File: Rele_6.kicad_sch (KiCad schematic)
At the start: 6 parts, among them J18 Rele_6, J36 Pin GND, K7 SRD-05VDC-SL-C, Q15 PMBT3904,235

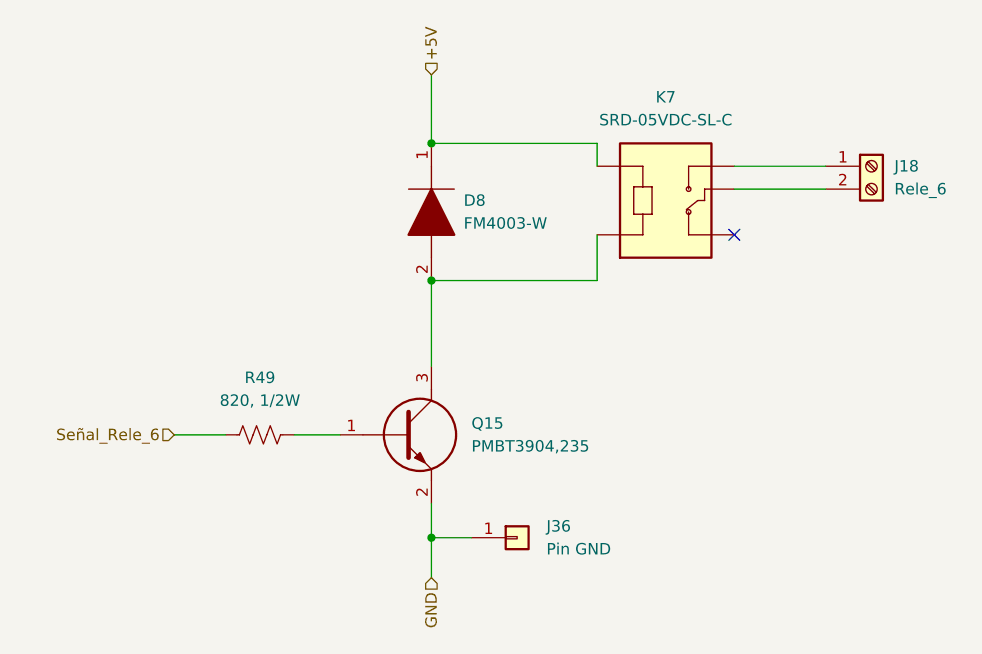
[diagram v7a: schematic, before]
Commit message: Se modificaron algunos componentes, según disponibilidad
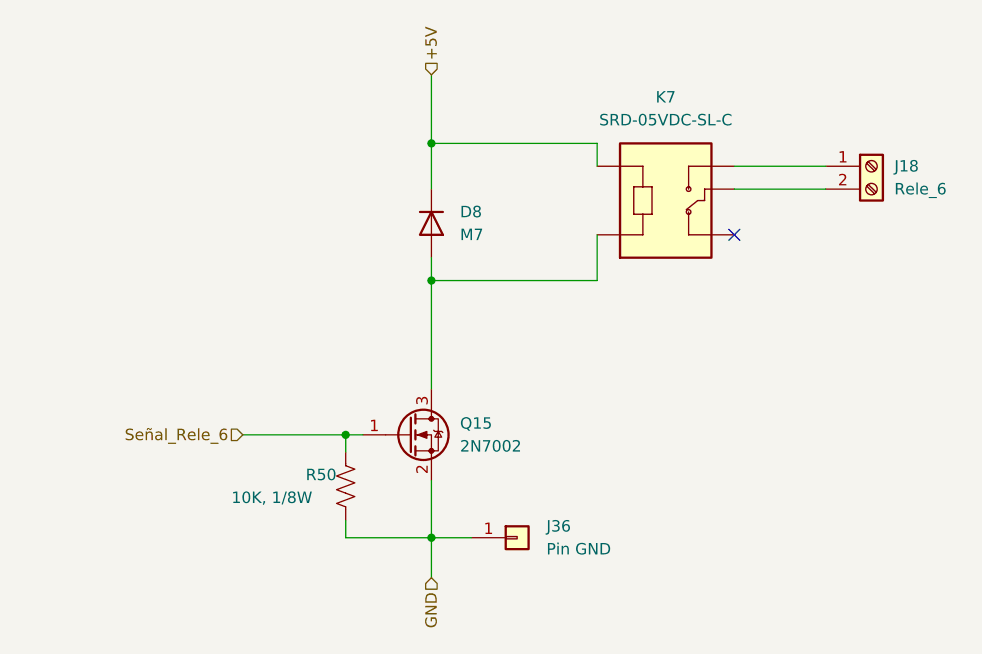
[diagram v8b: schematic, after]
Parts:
- removed D8: FM4003-W, FM4003W:DIOM5025X231N, symbol FM4003-W:FM4003-W
- removed Q15: PMBT3904,235, PMBT3904,235:SOT95P230X110-3N, symbol PMBT3904,235:PMBT3904,235
- removed R49: 820, 1/2W, Resistor_SMD:R_0805_2012Metric, symbol Device:R_US
- added D8: M7, Diode_SMD:D_SMA, symbol Device:D
- added Q15: 2N7002, Package_TO_SOT_SMD:SOT-23, symbol Transistor_FET:2N7002
- added R50: 10K, 1/8W, Resistor_SMD:R_0805_2012Metric, symbol Device:R_US
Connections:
- net +5V: now also D8.1 (K)
- net GND: now also Q15.2 (S), R50.2
- net Señal_Rele_6: now also Q15.1 (G), R50.1
- net at K7.A2: now also D8.2 (A), Q15.3 (D)
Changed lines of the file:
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@@
 (kicad_sch (version 20211123) (generator eeschema)
   (paper "A4")
+  (junction (at 137.16 107.315) (diameter 0) (color 0 0 0 0)
+  )
   (junction (at 146.685 118.745) (diameter 0) (color 0 0 0 0)
   )
+  (junction (at 146.685 90.17) (diameter 0) (color 0 0 0 0)
+  )
   (junction (at 146.685 74.93) (diameter 0) (color 0 0 0 0)
-  )
-  (junction (at 146.685 90.17) (diameter 0) (color 0 0 0 0)
   )
   (no_connect (at 180.34 85.09))
@@
     (stroke (width 0) (type default) (color 0 0 0 0))
   )
-  (wire (pts (xy 131.445 107.315) (xy 136.525 107.315))
+  (wire (pts (xy 137.16 116.84) (xy 137.16 118.745))
     (stroke (width 0) (type default) (color 0 0 0 0))
   )
-  (wire (pts (xy 146.685 114.935) (xy 146.685 118.745))
+  (wire (pts (xy 137.16 107.315) (xy 139.065 107.315))
+    (stroke (width 0) (type default) (color 0 0 0 0))
+  )
+  (wire (pts (xy 125.73 107.315) (xy 137.16 107.315))
+    (stroke (width 0) (type default) (color 0 0 0 0))
+  )
+  (wire (pts (xy 146.685 112.395) (xy 146.685 118.745))
     (stroke (width 0) (type default) (color 0 0 0 0))
   )
@@
     (stroke (width 0) (type default) (color 0 0 0 0))
   )
+  (wire (pts (xy 137.16 107.315) (xy 137.16 109.22))
+    (stroke (width 0) (type default) (color 0 0 0 0))
+  )
   (wire (pts (xy 146.685 67.31) (xy 146.685 74.93))
+    (stroke (width 0) (type default) (color 0 0 0 0))
+  )
+  (wire (pts (xy 146.685 74.93) (xy 146.685 80.01))
+    (stroke (width 0) (type default) (color 0 0 0 0))
+  )
+  (wire (pts (xy 146.685 87.63) (xy 146.685 90.17))
+    (stroke (width 0) (type default) (color 0 0 0 0))
+  )
+  (wire (pts (xy 137.16 118.745) (xy 146.685 118.745))
     (stroke (width 0) (type default) (color 0 0 0 0))
   )
@@
     (stroke (width 0) (type default) (color 0 0 0 0))
   )
-  (wire (pts (xy 118.11 107.315) (xy 123.825 107.315))
-    (stroke (width 0) (type default) (color 0 0 0 0))
-  )
-  (wire (pts (xy 146.685 90.17) (xy 146.685 99.695))
+  (wire (pts (xy 146.685 90.17) (xy 146.685 102.235))
     (stroke (width 0) (type default) (color 0 0 0 0))
   )
@@
     (effects (font (size 1.27 1.27)) (justify left))
   )
-  (hierarchical_label "Señal_Rele_6" (shape input) (at 118.11 107.315 180)
+  (hierarchical_label "Señal_Rele_6" (shape input) (at 125.73 107.315 180)
     (effects (font (size 1.27 1.27)) (justify right))
   )
-  (symbol (lib_id "Device:R_US") (at 127.635 107.315 90) (unit 1)
-    (in_bom yes) (on_board yes) (fields_autoplaced)
-    (property "Reference" "R49" (id 0) (at 127.635 100.965 90))
-    (property "Value" "820, 1/2W" (id 1) (at 127.635 103.505 90))
-    (property "Footprint" "Resistor_SMD:R_0805_2012Metric" (id 2) (at 127.889 106.299 90)
+  (symbol (lib_id "Device:R_US") (at 137.16 113.03 0) (unit 1)
+    (in_bom yes) (on_board yes)
+    (property "Reference" "R50" (id 0) (at 132.715 111.76 0)
+      (effects (font (size 1.27 1.27)) (justify left))
+    )
+    (property "Value" "10K, 1/8W" (id 1) (at 124.46 114.3 0)
+      (effects (font (size 1.27 1.27)) (justify left))
+    )
+    (property "Footprint" "Resistor_SMD:R_0805_2012Metric" (id 2) (at 138.176 113.284 90)
       (effects (font (size 1.27 1.27)) hide)
     )
-    (property "Datasheet" "~" (id 3) (at 127.635 107.315 0)
+    (property "Datasheet" "~" (id 3) (at 137.16 113.03 0)
       (effects (font (size 1.27 1.27)) hide)
     )
     (pin "1")
     (pin "2")
+  )
+  (symbol (lib_id "Transistor_FET:2N7002") (at 144.145 107.315 0) (unit 1)
+    (in_bom yes) (on_board yes) (fields_autoplaced)
+    (property "Reference" "Q15" (id 0) (at 149.86 106.0449 0)
+      (effects (font (size 1.27 1.27)) (justify left))
+    )
+    (property "Value" "2N7002" (id 1) (at 149.86 108.5849 0)
+      (effects (font (size 1.27 1.27)) (justify left))
+    )
+    (property "Footprint" "Package_TO_SOT_SMD:SOT-23" (id 2) (at 149.225 109.22 0)
+      (effects (font (size 1.27 1.27) italic) (justify left) hide)
+    )
+    (property "Datasheet" "https://www.onsemi.com/pub/Collateral/NDS7002A-D.PDF" (id 3) (at 144.145 107.315 0)
+      (effects (font (size 1.27 1.27)) (justify left) hide)
+    )
+    (pin "1")
+    (pin "2")
+    (pin "3")
   )
   (symbol (lib_id "Connector:Screw_Terminal_01x02") (at 195.58 77.47 0) (unit 1)
@@
     (pin "1")
     (pin "2")
-  )
-  (symbol (lib_id "FM4003-W:FM4003-W") (at 146.685 74.93 270) (unit 1)
-    (in_bom yes) (on_board yes) (fields_autoplaced)
-    (property "Reference" "D8" (id 0) (at 150.2664 81.2799 90)
-      (effects (font (size 1.27 1.27)) (justify left))
-    )
-    (property "Value" "FM4003-W" (id 1) (at 150.2664 83.8199 90)
-      (effects (font (size 1.27 1.27)) (justify left))
-    )
-    (property "Footprint" "FM4003W:DIOM5025X231N" (id 2) (at 146.685 86.36 0)
-      (effects (font (size 1.27 1.27)) (justify left) hide)
-    )
-    (property "Datasheet" "https://componentsearchengine.com/Datasheets/1/FM4003-W.pdf" (id 3) (at 144.145 86.36 0)
-      (effects (font (size 1.27 1.27)) (justify left) hide)
-    )
-    (property "Description" "Rectifiers 1A 200V GP" (id 4) (at 141.605 86.36 0)
-      (effects (font (size 1.27 1.27)) (justify left) hide)
-    )
-    (property "Height" "2.31" (id 5) (at 139.065 86.36 0)
-      (effects (font (size 1.27 1.27)) (justify left) hide)
-    )
-    (property "Manufacturer_Name" "Rectron" (id 6) (at 136.525 86.36 0)
-      (effects (font (size 1.27 1.27)) (justify left) hide)
-    )
-    (property "Manufacturer_Part_Number" "FM4003-W" (id 7) (at 133.985 86.36 0)
-      (effects (font (size 1.27 1.27)) (justify left) hide)
-    )
-    (property "Mouser Part Number" "583-FM4003-W" (id 8) (at 131.445 86.36 0)
-      (effects (font (size 1.27 1.27)) (justify left) hide)
-    )
-    (property "Mouser Price/Stock" "https://www.mouser.co.uk/ProductDetail/Rectron/FM4003-W/?qs=5h8Q3Z7TNRlJu6QU92Ho0w%3D%3D" (id 9) (at 128.905 86.36 0)
-      (effects (font (size 1.27 1.27)) (justify left) hide)
-    )
-    (property "Arrow Part Number" "FM4003-W" (id 10) (at 126.365 86.36 0)
-      (effects (font (size 1.27 1.27)) (justify left) hide)
-    )
-    (property "Arrow Price/Stock" "https://www.arrow.com/en/products/fm4003-w/rectron" (id 11) (at 123.825 86.36 0)
-      (effects (font (size 1.27 1.27)) (justify left) hide)
-    )
-    (property "Mouser Testing Part Number" "" (id 12) (at 121.285 86.36 0)
-      (effects (font (size 1.27 1.27)) (justify left) hide)
-    )
-    (property "Mouser Testing Price/Stock" "" (id 13) (at 118.745 86.36 0)
-      (effects (font (size 1.27 1.27)) (justify left) hide)
-    )
-    (pin "1")
-    (pin "2")
-  )
-  (symbol (lib_id "PMBT3904,235:PMBT3904,235") (at 136.525 107.315 0) (unit 1)
-    (in_bom yes) (on_board yes) (fields_autoplaced)
-    (property "Reference" "Q15" (id 0) (at 151.13 106.0449 0)
-      (effects (font (size 1.27 1.27)) (justify left))
-    )
-    (property "Value" "PMBT3904,235" (id 1) (at 151.13 108.5849 0)
-      (effects (font (size 1.27 1.27)) (justify left))
-    )
-    (property "Footprint" "PMBT3904,235:SOT95P230X110-3N" (id 2) (at 150.495 111.125 0)
-      (effects (font (size 1.27 1.27)) (justify left) hide)
-    )
-    (property "Datasheet" "https://assets.nexperia.com/documents/data-sheet/PMBT3904.pdf" (id 3) (at 150.495 113.665 0)
-      (effects (font (size 1.27 1.27)) (justify left) hide)
-    )
-    (property "Description" "PMBT3904 - NPN switching transistor" (id 4) (at 150.495 116.205 0)
-      (effects (font (size 1.27 1.27)) (justify left) hide)
-    )
-    (property "Height" "1.1" (id 5) (at 150.495 118.745 0)
-      (effects (font (size 1.27 1.27)) (justify left) hide)
-    )
-    (property "Manufacturer_Name" "Nexperia" (id 6) (at 150.495 121.285 0)
-      (effects (font (size 1.27 1.27)) (justify left) hide)
-    )
-    (property "Manufacturer_Part_Number" "PMBT3904,235" (id 7) (at 150.495 123.825 0)
-      (effects (font (size 1.27 1.27)) (justify left) hide)
-    )
-    (property "Mouser Part Number" "771-PMBT3904235" (id 8) (at 150.495 126.365 0)
-      (effects (font (size 1.27 1.27)) (justify left) hide)
-    )
-    (property "Mouser Price/Stock" "https://www.mouser.co.uk/ProductDetail/Nexperia/PMBT3904235?qs=LOCUfHb8d9uziIfl4fmvZg%3D%3D" (id 9) (at 150.495 128.905 0)
-      (effects (font (size 1.27 1.27)) (justify left) hide)
-    )
-    (property "Arrow Part Number" "PMBT3904,235" (id 10) (at 150.495 131.445 0)
-      (effects (font (size 1.27 1.27)) (justify left) hide)
-    )
-    (property "Arrow Price/Stock" "https://www.arrow.com/en/products/pmbt3904235/nexperia?region=nac" (id 11) (at 150.495 133.985 0)
-      (effects (font (size 1.27 1.27)) (justify left) hide)
-    )
-    (property "Mouser Testing Part Number" "" (id 12) (at 150.495 136.525 0)
-      (effects (font (size 1.27 1.27)) (justify left) hide)
-    )
-    (property "Mouser Testing Price/Stock" "" (id 13) (at 150.495 139.065 0)
-      (effects (font (size 1.27 1.27)) (justify left) hide)
-    )
-    (pin "1")
-    (pin "2")
-    (pin "3")
   )
   (symbol (lib_id "SRD-05VDC-SL-C:SRD-05VDC-SL-C") (at 172.72 80.01 0) (unit 1)
@@
     (pin "1")
   )
+  (symbol (lib_id "Device:D") (at 146.685 83.82 270) (unit 1)
+    (in_bom yes) (on_board yes) (fields_autoplaced)
+    (property "Reference" "D8" (id 0) (at 149.86 82.5499 90)
+      (effects (font (size 1.27 1.27)) (justify left))
+    )
+    (property "Value" "M7" (id 1) (at 149.86 85.0899 90)
+      (effects (font (size 1.27 1.27)) (justify left))
+    )
+    (property "Footprint" "Diode_SMD:D_SMA" (id 2) (at 146.685 83.82 0)
+      (effects (font (size 1.27 1.27)) hide)
+    )
+    (property "Datasheet" "~" (id 3) (at 146.685 83.82 0)
+      (effects (font (size 1.27 1.27)) hide)
+    )
+    (pin "1")
+    (pin "2")
+  )
 )
